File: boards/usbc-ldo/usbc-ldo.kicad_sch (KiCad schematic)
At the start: 12 parts, among them J1 USB-C, U1 AMS1117-3.3

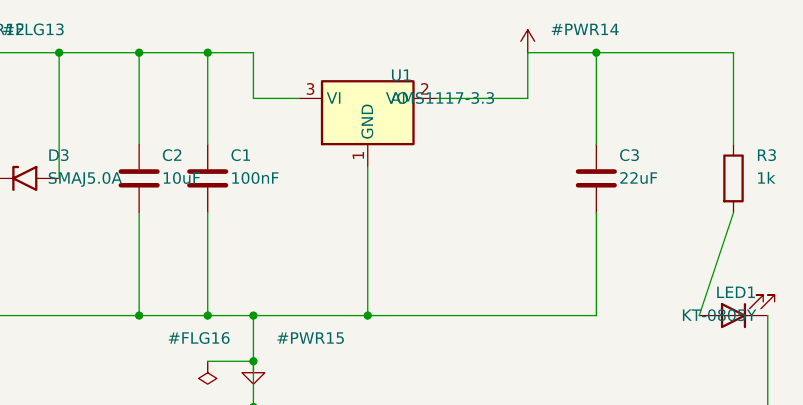
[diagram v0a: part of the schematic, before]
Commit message: usbc-ldo: LP38693MP-3.3 + 4.7uF caps (USB inrush and low-VBUS dropout fixed)
AMS1117 dropped out of regulation at USB's 4.4V minimum and C2 10uF + C3 22uF
injected 124 uC on hot-plug (USB 2.0 limit 50 uC). AP2112K fixed both but its
6.5V absolute max is below the simulated 6.77V hot-plug overshoot.
LP38693 (12V abs max, 0.33V dropout) passes all three; sim compares v1/v2/v3.
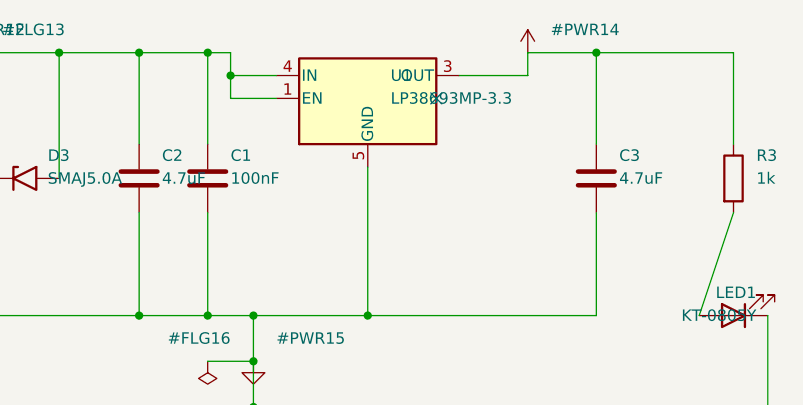
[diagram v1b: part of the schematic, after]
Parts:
- removed U1: AMS1117-3.3, Package_TO_SOT_SMD:SOT-223-3_TabPin2, symbol Regulator_Linear:AMS1117-3.3
- added U1: LP38693MP-3.3, Package_TO_SOT_SMD:SOT-223-5, symbol Regulator_Linear:LP38693MP-3.3
- C2: value 10uF -> 4.7uF
- C3: value 22uF -> 4.7uF
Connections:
- net +3V3: now also U1.3 (OUT)
- net +5V: now also U1.1 (EN), U1.4 (IN)
- net GND: now also U1.5 (GND)
- no-connect marks 4 -> 5
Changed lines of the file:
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@@
 	)
 	(wire
-		(pts (xy 129.54 82.55) (xy 124.46 82.55))
-		(stroke (width 0) (type default))
-	)
-	(wire
-		(pts (xy 124.46 82.55) (xy 124.46 77.47))
-		(stroke (width 0) (type default))
-	)
-	(wire
-		(pts (xy 144.78 82.55) (xy 154.94 82.55))
-		(stroke (width 0) (type default))
-	)
-	(wire
-		(pts (xy 154.94 82.55) (xy 154.94 77.47))
+		(pts (xy 127.0 80.01) (xy 121.92 80.01))
+		(stroke (width 0) (type default))
+	)
+	(wire
+		(pts (xy 121.92 80.01) (xy 121.92 77.47))
+		(stroke (width 0) (type default))
+	)
+	(wire
+		(pts (xy 127.0 82.55) (xy 121.92 82.55))
+		(stroke (width 0) (type default))
+	)
+	(wire
+		(pts (xy 121.92 82.55) (xy 121.92 80.01))
+		(stroke (width 0) (type default))
+	)
+	(wire
+		(pts (xy 147.32 80.01) (xy 154.94 80.01))
+		(stroke (width 0) (type default))
+	)
+	(wire
+		(pts (xy 154.94 80.01) (xy 154.94 77.47))
 		(stroke (width 0) (type default))
 	)
@@
 	)
 	(wire
-		(pts (xy 119.38 77.47) (xy 124.46 77.47))
+		(pts (xy 119.38 77.47) (xy 121.92 77.47))
 		(stroke (width 0) (type default))
 	)
@@
 	(junction
 		(at 119.38 106.68)
+		(diameter 0)
+		(color 0 0 0 0)
+	)
+	(junction
+		(at 121.92 80.01)
 		(diameter 0)
 		(color 0 0 0 0)
@@
 	(no_connect
 		(at 83.82 132.08)
+	)
+	(no_connect
+		(at 144.78 82.55)
 	)
 	(symbol
@@
 		(instances
 			(project ""
-				(path "/5f9ac0d2-1964-402b-bbdd-e34a80192436"
+				(path "/1831d799-2f6e-427d-b56f-e220eb21bc90"
 					(reference "J1")
 					(unit 1)
@@
 		(instances
 			(project ""
-				(path "/5f9ac0d2-1964-402b-bbdd-e34a80192436"
+				(path "/1831d799-2f6e-427d-b56f-e220eb21bc90"
 					(reference "D1")
 					(unit 1)
@@
 		(instances
 			(project ""
-				(path "/5f9ac0d2-1964-402b-bbdd-e34a80192436"
+				(path "/1831d799-2f6e-427d-b56f-e220eb21bc90"
 					(reference "R1")
 					(unit 1)
@@
 		(instances
 			(project ""
-				(path "/5f9ac0d2-1964-402b-bbdd-e34a80192436"
+				(path "/1831d799-2f6e-427d-b56f-e220eb21bc90"
 					(reference "R2")
 					(unit 1)
@@
 		(instances
 			(project ""
-				(path "/5f9ac0d2-1964-402b-bbdd-e34a80192436"
+				(path "/1831d799-2f6e-427d-b56f-e220eb21bc90"
 					(reference "D2")
 					(unit 1)
@@
 		(instances
 			(project ""
-				(path "/5f9ac0d2-1964-402b-bbdd-e34a80192436"
+				(path "/1831d799-2f6e-427d-b56f-e220eb21bc90"
 					(reference "D3")
 					(unit 1)
@@
 			(effects (font (size 1.27 1.27)) (justify left))
 		)
-		(property "Value" "10uF"
+		(property "Value" "4.7uF"
 			(at 114.30000000000001 91.44 0)
 			(effects (font (size 1.27 1.27)) (justify left))
@@
 		(instances
 			(project ""
-				(path "/5f9ac0d2-1964-402b-bbdd-e34a80192436"
+				(path "/1831d799-2f6e-427d-b56f-e220eb21bc90"
 					(reference "C2")
 					(unit 1)
@@
 	)
 	(symbol
-		(lib_id "Regulator_Linear:AMS1117-3.3")
+		(lib_id "Regulator_Linear:LP38693MP-3.3")
 		(at 137.16 82.55 0)
 		(unit 1)
@@
 			(effects (font (size 1.27 1.27)) (justify left))
 		)
-		(property "Value" "AMS1117-3.3"
+		(property "Value" "LP38693MP-3.3"
 			(at 139.7 82.55 0)
 			(effects (font (size 1.27 1.27)) (justify left))
 		)
-		(property "Footprint" "Package_TO_SOT_SMD:SOT-223-3_TabPin2"
+		(property "Footprint" "Package_TO_SOT_SMD:SOT-223-5"
 			(at 137.16 82.55 0)
 			(effects (font (size 1.27 1.27)) (hide yes))
@@
 		(pin "2")
 		(pin "3")
-		(instances
-			(project ""
-				(path "/5f9ac0d2-1964-402b-bbdd-e34a80192436"
+		(pin "4")
+		(pin "5")
+		(instances
+			(project ""
+				(path "/1831d799-2f6e-427d-b56f-e220eb21bc90"
 					(reference "U1")
 					(unit 1)
@@
 		(instances
 			(project ""
-				(path "/5f9ac0d2-1964-402b-bbdd-e34a80192436"
+				(path "/1831d799-2f6e-427d-b56f-e220eb21bc90"
 					(reference "C1")
 					(unit 1)
@@
 			(effects (font (size 1.27 1.27)) (justify left))
 		)
-		(property "Value" "22uF"
+		(property "Value" "4.7uF"
 			(at 165.1 91.44 0)
 			(effects (font (size 1.27 1.27)) (justify left))
@@
 		(instances
 			(project ""
-				(path "/5f9ac0d2-1964-402b-bbdd-e34a80192436"
+				(path "/1831d799-2f6e-427d-b56f-e220eb21bc90"
 					(reference "C3")
 					(unit 1)
@@
 		(instances
 			(project ""
-				(path "/5f9ac0d2-1964-402b-bbdd-e34a80192436"
+				(path "/1831d799-2f6e-427d-b56f-e220eb21bc90"
 					(reference "R3")
 					(unit 1)
@@
 		(instances
 			(project ""
-				(path "/5f9ac0d2-1964-402b-bbdd-e34a80192436"
+				(path "/1831d799-2f6e-427d-b56f-e220eb21bc90"
 					(reference "LED1")
 					(unit 1)
@@
 		(instances
 			(project ""
-				(path "/5f9ac0d2-1964-402b-bbdd-e34a80192436"
+				(path "/1831d799-2f6e-427d-b56f-e220eb21bc90"
 					(reference "#PWR12")
 					(unit 1)
@@
 		(instances
 			(project ""
-				(path "/5f9ac0d2-1964-402b-bbdd-e34a80192436"
+				(path "/1831d799-2f6e-427d-b56f-e220eb21bc90"
 					(reference "#FLG13")
 					(unit 1)
@@
 		(instances
 			(project ""
-				(path "/5f9ac0d2-1964-402b-bbdd-e34a80192436"
+				(path "/1831d799-2f6e-427d-b56f-e220eb21bc90"
 					(reference "#PWR14")
 					(unit 1)
@@
 		(instances
 			(project ""
-				(path "/5f9ac0d2-1964-402b-bbdd-e34a80192436"
+				(path "/1831d799-2f6e-427d-b56f-e220eb21bc90"
 					(reference "#PWR15")
 					(unit 1)
@@
 		(instances
 			(project ""
-				(path "/5f9ac0d2-1964-402b-bbdd-e34a80192436"
+				(path "/1831d799-2f6e-427d-b56f-e220eb21bc90"
 					(reference "#FLG16")
 					(unit 1)

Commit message: fab: Gerber/drill zip + JLCPCB BOM/CPL with self-checks; USBLC6-2SC6 to match SOT-23-6
lib/fab.py runs as the last build step on all three boards. It refuses to
write the zip when a required Gerber layer is missing or empty, when the
drill-hit count differs from vias + plated/NPTH pad holes (route-format
slots counted once), or when BOM / CPL / board refdes sets disagree.

It also compares each symbol's library default footprint with the one
actually assigned. That caught all three boards using the USBLC6-2P6
symbol (SOT-666) on a SOT-23-6 footprint: electrically identical pinout,
so ERC/DRC/netlist checks passed, but a BOM ordered by value would buy a
part that does not fit. Switched to USBLC6-2SC6.

LCSC part numbers come from a hand-checked boards/<b>/lcsc.json; the
script never guesses them and lists missing rows in fab/missing-lcsc.txt.
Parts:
- removed D2: USBLC6-2P6, Package_TO_SOT_SMD:SOT-23-6, symbol Power_Protection:USBLC6-2P6
- added D2: USBLC6-2SC6, Package_TO_SOT_SMD:SOT-23-6, symbol Power_Protection:USBLC6-2SC6
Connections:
- net +5V: now also D2.5 (VBUS)
- net GND: now also D2.2 (GND)
- net at J1.A6 (D+), J1.B6 (D+): now also D2.1 (I/O1)
- net at J1.A7 (D-), J1.B7 (D-): now also D2.3 (I/O2)
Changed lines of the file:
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@@
 		(instances
 			(project ""
-				(path "/1831d799-2f6e-427d-b56f-e220eb21bc90"
+				(path "/bec73b27-2021-4d36-b13e-9337feb9ca5a"
 					(reference "J1")
 					(unit 1)
@@
 		(instances
 			(project ""
-				(path "/1831d799-2f6e-427d-b56f-e220eb21bc90"
+				(path "/bec73b27-2021-4d36-b13e-9337feb9ca5a"
 					(reference "D1")
 					(unit 1)
@@
 		(instances
 			(project ""
-				(path "/1831d799-2f6e-427d-b56f-e220eb21bc90"
+				(path "/bec73b27-2021-4d36-b13e-9337feb9ca5a"
 					(reference "R1")
 					(unit 1)
@@
 		(instances
 			(project ""
-				(path "/1831d799-2f6e-427d-b56f-e220eb21bc90"
+				(path "/bec73b27-2021-4d36-b13e-9337feb9ca5a"
 					(reference "R2")
 					(unit 1)
@@
 	)
 	(symbol
-		(lib_id "Power_Protection:USBLC6-2P6")
+		(lib_id "Power_Protection:USBLC6-2SC6")
 		(at 78.74 132.08 0)
 		(unit 1)
@@
 			(effects (font (size 1.27 1.27)) (justify left))
 		)
-		(property "Value" "USBLC6-2P6"
+		(property "Value" "USBLC6-2SC6"
 			(at 81.28 132.08 0)
 			(effects (font (size 1.27 1.27)) (justify left))
@@
 		(instances
 			(project ""
-				(path "/1831d799-2f6e-427d-b56f-e220eb21bc90"
+				(path "/bec73b27-2021-4d36-b13e-9337feb9ca5a"
 					(reference "D2")
 					(unit 1)
@@
 		(instances
 			(project ""
-				(path "/1831d799-2f6e-427d-b56f-e220eb21bc90"
+				(path "/bec73b27-2021-4d36-b13e-9337feb9ca5a"
 					(reference "D3")
 					(unit 1)
@@
 		(instances
 			(project ""
-				(path "/1831d799-2f6e-427d-b56f-e220eb21bc90"
+				(path "/bec73b27-2021-4d36-b13e-9337feb9ca5a"
 					(reference "C2")
 					(unit 1)
@@
 		(instances
 			(project ""
-				(path "/1831d799-2f6e-427d-b56f-e220eb21bc90"
+				(path "/bec73b27-2021-4d36-b13e-9337feb9ca5a"
 					(reference "U1")
 					(unit 1)
@@
 		(instances
 			(project ""
-				(path "/1831d799-2f6e-427d-b56f-e220eb21bc90"
+				(path "/bec73b27-2021-4d36-b13e-9337feb9ca5a"
 					(reference "C1")
 					(unit 1)
@@
 		(instances
 			(project ""
-				(path "/1831d799-2f6e-427d-b56f-e220eb21bc90"
+				(path "/bec73b27-2021-4d36-b13e-9337feb9ca5a"
 					(reference "C3")
 					(unit 1)
@@
 		(instances
 			(project ""
-				(path "/1831d799-2f6e-427d-b56f-e220eb21bc90"
+				(path "/bec73b27-2021-4d36-b13e-9337feb9ca5a"
 					(reference "R3")
 					(unit 1)
@@
 		(instances
 			(project ""
-				(path "/1831d799-2f6e-427d-b56f-e220eb21bc90"
+				(path "/bec73b27-2021-4d36-b13e-9337feb9ca5a"
 					(reference "LED1")
 					(unit 1)
@@
 		(instances
 			(project ""
-				(path "/1831d799-2f6e-427d-b56f-e220eb21bc90"
+				(path "/bec73b27-2021-4d36-b13e-9337feb9ca5a"
 					(reference "#PWR12")
 					(unit 1)
@@
 		(instances
 			(project ""
-				(path "/1831d799-2f6e-427d-b56f-e220eb21bc90"
+				(path "/bec73b27-2021-4d36-b13e-9337feb9ca5a"
 					(reference "#FLG13")
 					(unit 1)
@@
 		(instances
 			(project ""
-				(path "/1831d799-2f6e-427d-b56f-e220eb21bc90"
+				(path "/bec73b27-2021-4d36-b13e-9337feb9ca5a"
 					(reference "#PWR14")
 					(unit 1)
@@
 		(instances
 			(project ""
-				(path "/1831d799-2f6e-427d-b56f-e220eb21bc90"
+				(path "/bec73b27-2021-4d36-b13e-9337feb9ca5a"
 					(reference "#PWR15")
 					(unit 1)
@@
 		(instances
 			(project ""
-				(path "/1831d799-2f6e-427d-b56f-e220eb21bc90"
+				(path "/bec73b27-2021-4d36-b13e-9337feb9ca5a"
 					(reference "#FLG16")
 					(unit 1)

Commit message: review: datasheet design review on the netlist; fixes a reversed TVS and dim LEDs
lib/review.py checks the design intent that ERC and the netlist check take
on trust: diode/TVS polarity against inferred rail voltages, LED current
from the JLC Vf range, per-datasheet decoupling and supply ranges, USB-C
CC pull-downs and D+/D- on both sides, ESP32-C3 EN RC, strapping pins and
GPIO18/19, relay flyback path and pickup voltage, capacitor rating and
polarity. It runs after the netlist check and stops the build on ERROR.
lib/review_test.py breaks the real netlists 15 ways; every rule fires and
the unmodified boards report no ERROR.

Real defects it found:
- usbc-ldo: SMAJ5.0A had anode on +5V and cathode on GND (KiCad names
  the cathode pin "A1"), shorting the rail on plug-in. Swapped.
- esp32c3: blue user LED on a 3.3 V GPIO (Vf 2.5-3.6 V) -> yellow, 470R.
- esp32c3, relay8: green power LED at ~0.45 mA through 1k -> 220R.
- usbc-ldo: SS32 symbol for an SS34 part -> Diode:SS34.

Also: lcsc-check.json keeps JLC attributes (Vf, voltage rating) for the
review; lcsc.py groups parts from net.txt instead of fab/groups.json; the
build retries freerouting (up to 3 runs) because it is not deterministic
and occasionally leaves two connections unrouted on the same DSN.
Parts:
- removed D1: SS34, Diode_SMD:D_SMA, symbol Diode:SS32
- added D1: SS34, Diode_SMD:D_SMA, symbol Diode:SS34
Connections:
- net +5V: now also D3.1 (A1), D1.1 (K); no longer D3.2 (A2)
- net GND: now also D3.2 (A2); no longer D3.1 (A1)
- net at J1.A4 (VBUS), J1.A9 (VBUS), J1.B4 (VBUS)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: now also D1.2 (A)
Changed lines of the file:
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@@
 	)
 	(wire
-		(pts (xy 102.87 91.44) (xy 102.87 77.47))
-		(stroke (width 0) (type default))
-	)
-	(wire
-		(pts (xy 95.25 91.44) (xy 95.25 106.68))
+		(pts (xy 95.25 91.44) (xy 95.25 77.47))
+		(stroke (width 0) (type default))
+	)
+	(wire
+		(pts (xy 102.87 91.44) (xy 102.87 106.68))
 		(stroke (width 0) (type default))
 	)
@@
 	)
 	(wire
-		(pts (xy 93.98 77.47) (xy 102.87 77.47))
-		(stroke (width 0) (type default))
-	)
-	(wire
-		(pts (xy 102.87 77.47) (xy 111.76 77.47))
+		(pts (xy 93.98 77.47) (xy 95.25 77.47))
+		(stroke (width 0) (type default))
+	)
+	(wire
+		(pts (xy 95.25 77.47) (xy 111.76 77.47))
 		(stroke (width 0) (type default))
 	)
@@
 	)
 	(wire
-		(pts (xy 95.25 106.68) (xy 162.56 106.68))
+		(pts (xy 102.87 106.68) (xy 162.56 106.68))
 		(stroke (width 0) (type default))
 	)
@@
 	)
 	(junction
-		(at 102.87 77.47)
+		(at 95.25 77.47)
 		(diameter 0)
 		(color 0 0 0 0)
@@
 		(instances
 			(project ""
-				(path "/5baa53b7-78ef-48ce-8ca6-8f948bab0c8e"
+				(path "/19fb1582-cab7-473f-ba64-59e157790817"
 					(reference "J1")
 					(unit 1)
@@
 	)
 	(symbol
-		(lib_id "Diode:SS32")
+		(lib_id "Diode:SS34")
 		(at 78.74 82.55 180)
 		(unit 1)
@@
 		(instances
 			(project ""
-				(path "/5baa53b7-78ef-48ce-8ca6-8f948bab0c8e"
+				(path "/19fb1582-cab7-473f-ba64-59e157790817"
 					(reference "D1")
 					(unit 1)
@@
 		(instances
 			(project ""
-				(path "/5baa53b7-78ef-48ce-8ca6-8f948bab0c8e"
+				(path "/19fb1582-cab7-473f-ba64-59e157790817"
 					(reference "R1")
 					(unit 1)
@@
 		(instances
 			(project ""
-				(path "/5baa53b7-78ef-48ce-8ca6-8f948bab0c8e"
+				(path "/19fb1582-cab7-473f-ba64-59e157790817"
 					(reference "R2")
 					(unit 1)
@@
 		(instances
 			(project ""
-				(path "/5baa53b7-78ef-48ce-8ca6-8f948bab0c8e"
+				(path "/19fb1582-cab7-473f-ba64-59e157790817"
 					(reference "D2")
 					(unit 1)
@@
 		(instances
 			(project ""
-				(path "/5baa53b7-78ef-48ce-8ca6-8f948bab0c8e"
+				(path "/19fb1582-cab7-473f-ba64-59e157790817"
 					(reference "D3")
 					(unit 1)
@@
 		(instances
 			(project ""
-				(path "/5baa53b7-78ef-48ce-8ca6-8f948bab0c8e"
+				(path "/19fb1582-cab7-473f-ba64-59e157790817"
 					(reference "C2")
 					(unit 1)
@@
 		(instances
 			(project ""
-				(path "/5baa53b7-78ef-48ce-8ca6-8f948bab0c8e"
+				(path "/19fb1582-cab7-473f-ba64-59e157790817"
 					(reference "U1")
 					(unit 1)
@@
 		(instances
 			(project ""
-				(path "/5baa53b7-78ef-48ce-8ca6-8f948bab0c8e"
+				(path "/19fb1582-cab7-473f-ba64-59e157790817"
 					(reference "C1")
 					(unit 1)
@@
 		(instances
 			(project ""
-				(path "/5baa53b7-78ef-48ce-8ca6-8f948bab0c8e"
+				(path "/19fb1582-cab7-473f-ba64-59e157790817"
 					(reference "C3")
 					(unit 1)
@@
 		(instances
 			(project ""
-				(path "/5baa53b7-78ef-48ce-8ca6-8f948bab0c8e"
+				(path "/19fb1582-cab7-473f-ba64-59e157790817"
 					(reference "R3")
 					(unit 1)
@@
 		(instances
 			(project ""
-				(path "/5baa53b7-78ef-48ce-8ca6-8f948bab0c8e"
+				(path "/19fb1582-cab7-473f-ba64-59e157790817"
 					(reference "LED1")
 					(unit 1)
@@
 		(instances
 			(project ""
-				(path "/5baa53b7-78ef-48ce-8ca6-8f948bab0c8e"
+				(path "/19fb1582-cab7-473f-ba64-59e157790817"
 					(reference "#PWR12")
 					(unit 1)
@@
 		(instances
 			(project ""
-				(path "/5baa53b7-78ef-48ce-8ca6-8f948bab0c8e"
+				(path "/19fb1582-cab7-473f-ba64-59e157790817"
 					(reference "#FLG13")
 					(unit 1)
@@
 		(instances
 			(project ""
-				(path "/5baa53b7-78ef-48ce-8ca6-8f948bab0c8e"
+				(path "/19fb1582-cab7-473f-ba64-59e157790817"
 					(reference "#PWR14")
 					(unit 1)
@@
 		(instances
 			(project ""
-				(path "/5baa53b7-78ef-48ce-8ca6-8f948bab0c8e"
+				(path "/19fb1582-cab7-473f-ba64-59e157790817"
 					(reference "#PWR15")
 					(unit 1)
@@
 		(instances
 			(project ""
-				(path "/5baa53b7-78ef-48ce-8ca6-8f948bab0c8e"
+				(path "/19fb1582-cab7-473f-ba64-59e157790817"
 					(reference "#FLG16")
 					(unit 1)
